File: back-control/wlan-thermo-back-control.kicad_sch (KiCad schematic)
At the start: 12 parts, among them J1 AC / L, J2 AC / N, J3 Signal, J4 Front PWR, Q1 SS8050-G, U2 WX-DC12003, U3 PC817

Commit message: First version fitting together
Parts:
- J1: footprint TerminalBlock:TerminalBlock_bornier-3_P5.08mm -> Chof747 Footprints:TerminalBlock_2_P10.16mm; symbol Connector:Conn_01x03_Socket -> Connector:Conn_01x02_Socket
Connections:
- net L: now also J1.2 (Pin_2); no longer J1.3 (Pin_3)
- no-connect marks 1 -> 0
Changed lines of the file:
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@@
   (junction (at 138.43 107.95) (diameter 0) (color 0 0 0 0)
   )
-  (no_connect (at 147.32 105.41))
   (wire (pts (xy 138.43 107.95) (xy 147.32 107.95))
     (stroke (width 0) (type default))
@@
     (stroke (width 0) (type default))
   )
-  (wire (pts (xy 144.78 102.87) (xy 147.32 102.87))
+  (wire (pts (xy 144.78 105.41) (xy 147.32 105.41))
     (stroke (width 0) (type default))
   )
@@
     (stroke (width 0) (type default))
   )
-  (wire (pts (xy 144.78 97.79) (xy 144.78 102.87))
+  (wire (pts (xy 144.78 97.79) (xy 144.78 105.41))
     (stroke (width 0) (type default))
   )
@@
     )
   )
-  (symbol (lib_id "Connector:Conn_01x03_Socket") (at 152.4 105.41 0) (unit 1)
+  (symbol (lib_id "Connector:Conn_01x02_Socket") (at 152.4 105.41 0) (unit 1)
     (in_bom yes) (on_board yes) (dnp no)
     (property "Reference" "J1" (at 153.67 106.045 0)
@@
       (effects (font (size 1.27 1.27)) (justify left))
     )
-    (property "Footprint" "TerminalBlock:TerminalBlock_bornier-3_P5.08mm" (at 152.4 105.41 0)
+    (property "Footprint" "Chof747 Footprints:TerminalBlock_2_P10.16mm" (at 152.4 105.41 0)
       (effects (font (size 1.27 1.27)) hide)
     )
@@
     (pin "1")
     (pin "2")
-    (pin "3")
-    (instances
-      (project "wlan-thermo-back-control"
+    (instances
+      (project "wlan-thermo-back-control"

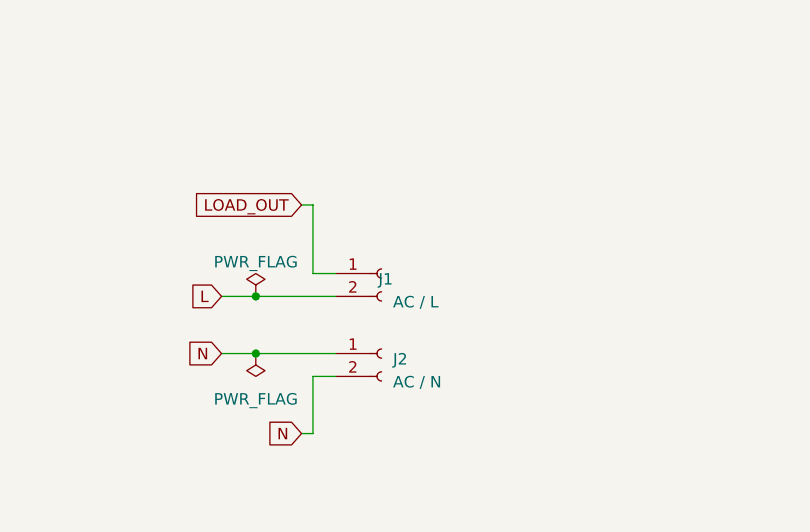
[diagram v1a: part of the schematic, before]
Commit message: Corrected wrongly placed footprint for relay
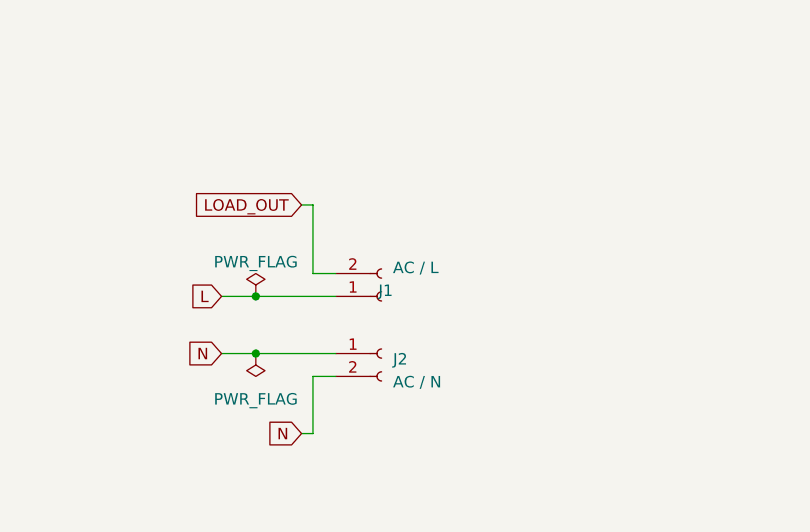
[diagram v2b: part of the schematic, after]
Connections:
- net L: now also J1.1 (Pin_1); no longer J1.2 (Pin_2)
- net LOAD_OUT: now also J1.2 (Pin_2); no longer J1.1 (Pin_1)
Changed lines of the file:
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@@
   (junction (at 138.43 107.95) (diameter 0) (color 0 0 0 0)
   )
+  (wire (pts (xy 38.1 114.3) (xy 38.1 118.11))
+    (stroke (width 0) (type default))
+  )
+  (wire (pts (xy 44.45 40.64) (xy 44.45 58.42))
+    (stroke (width 0) (type default))
+  )
+  (wire (pts (xy 144.78 105.41) (xy 147.32 105.41))
+    (stroke (width 0) (type default))
+  )
+  (wire (pts (xy 149.86 46.99) (xy 153.67 46.99))
+    (stroke (width 0) (type default))
+  )
+  (wire (pts (xy 22.86 41.91) (xy 22.86 48.26))
+    (stroke (width 0) (type default))
+  )
+  (wire (pts (xy 77.47 52.07) (xy 82.55 52.07))
+    (stroke (width 0) (type default))
+  )
+  (wire (pts (xy 63.5 40.64) (xy 66.04 40.64))
+    (stroke (width 0) (type default))
+  )
+  (wire (pts (xy 81.28 30.48) (xy 81.28 22.86))
+    (stroke (width 0) (type default))
+  )
+  (wire (pts (xy 69.85 52.07) (xy 63.5 52.07))
+    (stroke (width 0) (type default))
+  )
+  (wire (pts (xy 38.1 114.3) (xy 41.91 114.3))
+    (stroke (width 0) (type default))
+  )
+  (wire (pts (xy 149.86 49.53) (xy 153.67 49.53))
+    (stroke (width 0) (type default))
+  )
+  (wire (pts (xy 153.67 49.53) (xy 153.67 52.07))
+    (stroke (width 0) (type default))
+  )
   (wire (pts (xy 138.43 107.95) (xy 147.32 107.95))
     (stroke (width 0) (type default))
   )
-  (wire (pts (xy 38.1 114.3) (xy 38.1 118.11))
-    (stroke (width 0) (type default))
-  )
-  (wire (pts (xy 44.45 40.64) (xy 44.45 58.42))
-    (stroke (width 0) (type default))
-  )
-  (wire (pts (xy 149.86 46.99) (xy 153.67 46.99))
-    (stroke (width 0) (type default))
-  )
-  (wire (pts (xy 22.86 41.91) (xy 22.86 48.26))
-    (stroke (width 0) (type default))
-  )
-  (wire (pts (xy 77.47 52.07) (xy 82.55 52.07))
-    (stroke (width 0) (type default))
-  )
-  (wire (pts (xy 63.5 40.64) (xy 66.04 40.64))
-    (stroke (width 0) (type default))
-  )
-  (wire (pts (xy 81.28 30.48) (xy 81.28 22.86))
-    (stroke (width 0) (type default))
-  )
-  (wire (pts (xy 69.85 52.07) (xy 63.5 52.07))
-    (stroke (width 0) (type default))
-  )
-  (wire (pts (xy 38.1 114.3) (xy 41.91 114.3))
-    (stroke (width 0) (type default))
-  )
-  (wire (pts (xy 149.86 49.53) (xy 153.67 49.53))
-    (stroke (width 0) (type default))
-  )
-  (wire (pts (xy 153.67 49.53) (xy 153.67 52.07))
-    (stroke (width 0) (type default))
-  )
   (wire (pts (xy 134.62 107.95) (xy 138.43 107.95))
     (stroke (width 0) (type default))
@@
   )
   (wire (pts (xy 38.1 111.76) (xy 41.91 111.76))
-    (stroke (width 0) (type default))
-  )
-  (wire (pts (xy 144.78 105.41) (xy 147.32 105.41))
     (stroke (width 0) (type default))
   )
@@
     )
   )
-  (symbol (lib_id "Connector:Conn_01x02_Socket") (at 152.4 105.41 0) (unit 1)
+  (symbol (lib_id "Connector:Conn_01x02_Socket") (at 152.4 107.95 0) (mirror x) (unit 1)
     (in_bom yes) (on_board yes) (dnp no)
-    (property "Reference" "J1" (at 153.67 106.045 0)
+    (property "Reference" "J1" (at 153.67 107.315 0)
       (effects (font (size 1.27 1.27)) (justify right))
     )
-    (property "Value" "AC / L" (at 153.67 108.585 0)
-      (effects (font (size 1.27 1.27)) (justify left))
-    )
-    (property "Footprint" "Chof747 Footprints:TerminalBlock_2_P10.16mm" (at 152.4 105.41 0)
-      (effects (font (size 1.27 1.27)) hide)
-    )
-    (property "Datasheet" "~" (at 152.4 105.41 0)
-      (effects (font (size 1.27 1.27)) hide)
-    )
+    (property "Value" "AC / L" (at 153.67 104.775 0)
+      (effects (font (size 1.27 1.27)) (justify left))
+    )
+    (property "Footprint" "Chof747 Footprints:TerminalBlock_2_P10.16mm" (at 152.4 107.95 0)
+      (effects (font (size 1.27 1.27)) hide)
+    )
+    (property "Datasheet" "~" (at 152.4 107.95 0)
+      (effects (font (size 1.27 1.27)) hide)
+    )

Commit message: Revised optocopler footprint
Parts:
- U3: footprint Package_SO:SOP-4_3.8x4.1mm_P2.54mm -> Chof747 Footprints:SOP-4_6.7x4.1mm_P2.54mm
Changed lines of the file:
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@@
       (effects (font (size 1.27 1.27)))
     )
-    (property "Footprint" "Package_SO:SOP-4_3.8x4.1mm_P2.54mm" (at 31.75 66.04 0)
+    (property "Footprint" "Chof747 Footprints:SOP-4_6.7x4.1mm_P2.54mm" (at 31.75 66.04 0)
       (effects (font (size 1.27 1.27) italic) (justify left) hide)
     )

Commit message: Redid whole for creeping protection of power supply
- Changed frontend connectors also to throughole pins
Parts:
- J3, J4: footprint Connector_PinSocket_2.54mm:PinSocket_1x02_P2.54mm_Vertical_SMD_Pin1Right -> Connector_PinSocket_2.54mm:PinSocket_1x02_P2.54mm_Vertical
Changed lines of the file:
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@@
       (effects (font (size 1.27 1.27)) (justify left))
     )
-    (property "Footprint" "Connector_PinSocket_2.54mm:PinSocket_1x02_P2.54mm_Vertical_SMD_Pin1Right" (at 46.99 114.3 0)
+    (property "Footprint" "Connector_PinSocket_2.54mm:PinSocket_1x02_P2.54mm_Vertical" (at 46.99 114.3 0)
       (effects (font (size 1.27 1.27)) hide)
     )
@@
       (effects (font (size 1.27 1.27)) (justify left))
     )
-    (property "Footprint" "Connector_PinSocket_2.54mm:PinSocket_1x02_P2.54mm_Vertical_SMD_Pin1Right" (at 77.47 114.3 0)
+    (property "Footprint" "Connector_PinSocket_2.54mm:PinSocket_1x02_P2.54mm_Vertical" (at 77.47 114.3 0)
       (effects (font (size 1.27 1.27)) hide)
     )

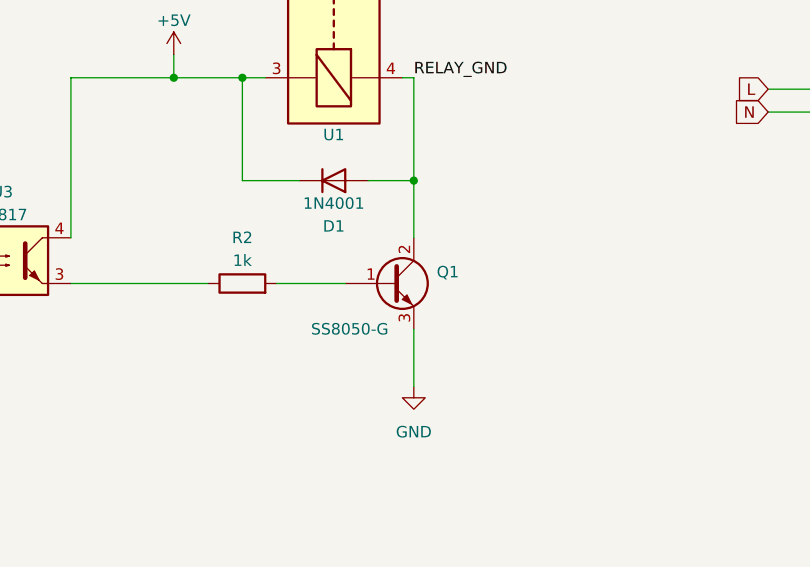
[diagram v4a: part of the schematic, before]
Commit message: Correcrted relay switching transistor pins
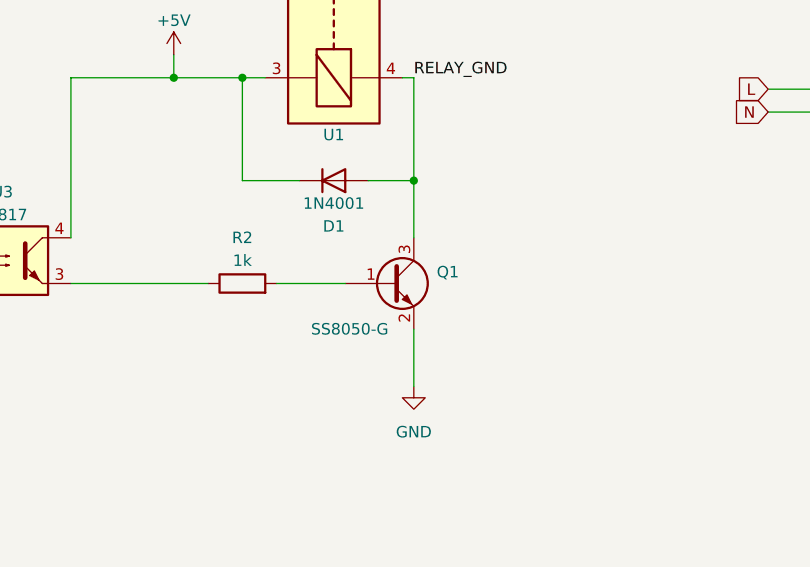
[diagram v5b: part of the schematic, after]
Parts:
- Q1: symbol Device:Q_NPN_BCE -> Device:Q_NPN_BEC
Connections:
- net GND: now also Q1.2 (E); no longer Q1.3 (E)
- net RELAY_GND: now also Q1.3 (C); no longer Q1.2 (C)
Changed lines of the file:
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@@
     )
   )
-  (symbol (lib_id "Device:Q_NPN_BCE") (at 80.01 63.5 0) (unit 1)
+  (symbol (lib_id "Device:Q_NPN_BEC") (at 80.01 63.5 0) (unit 1)
     (in_bom yes) (on_board yes) (dnp no)
     (property "Reference" "Q1" (at 85.09 62.2299 0)

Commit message: upgrade to  KiCad 8.0
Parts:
- D1: footprint Diode_SMD:D_SOD-123F -> Diode_THT:D_DO-41_SOD81_P10.16mm_Horizontal
- U3: footprint Chof747 Footprints:SOP-4_6.7x4.1mm_P2.54mm -> Package_DIP:DIP-4_W7.62mm
